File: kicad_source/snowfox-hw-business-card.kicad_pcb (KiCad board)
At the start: 2 copper layers, 85 x 54 mm, 114 parts, among them CN1 MEM2061-01-188-00-A, CN2 FSH-105-04-L-DH-SL, CN3 SFV24R-3STBE1HLF, CN4 10118192-0001LF, CN5 CONN_01X14, CN6 CONN_01X04, Q1 SI1308EDL, Q2 BC847, SW1 PTS 647 SK38 SMTR2 LFS, SW2 TAST_VER, SW3 PTS636 SL43 SMTR LFS, SW4 PTS 647 SK38 SMTR2 LFS, SW5 SWITCH_INV, U1 W25Q80D, U2 ATECC608A, U3 FE310-G002, U4 FT230XS, U5 TPS73633DBV, U6 TPS73618DBV, U7 M24LR, U8 BMA253, Y1 FA-238 16.0000MB-C3

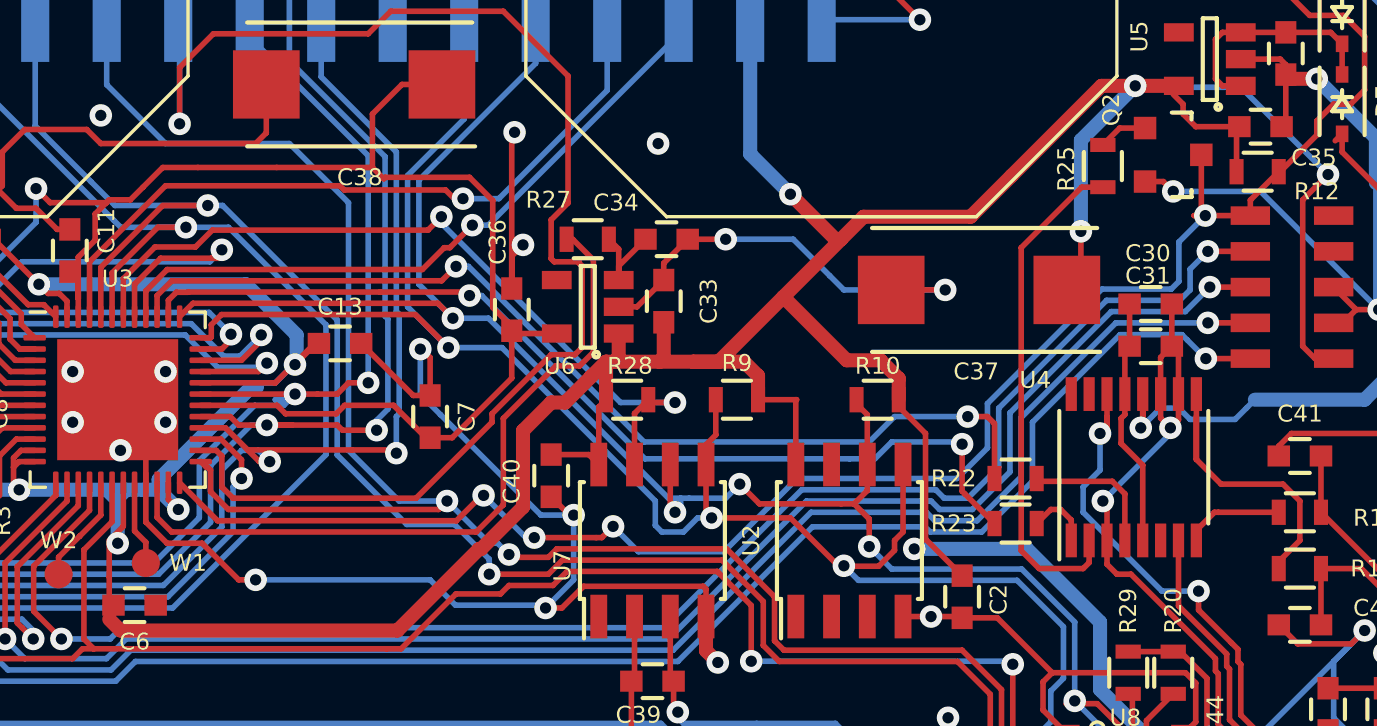
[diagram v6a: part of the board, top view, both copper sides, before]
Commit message: reworked reset circuit at usb serial
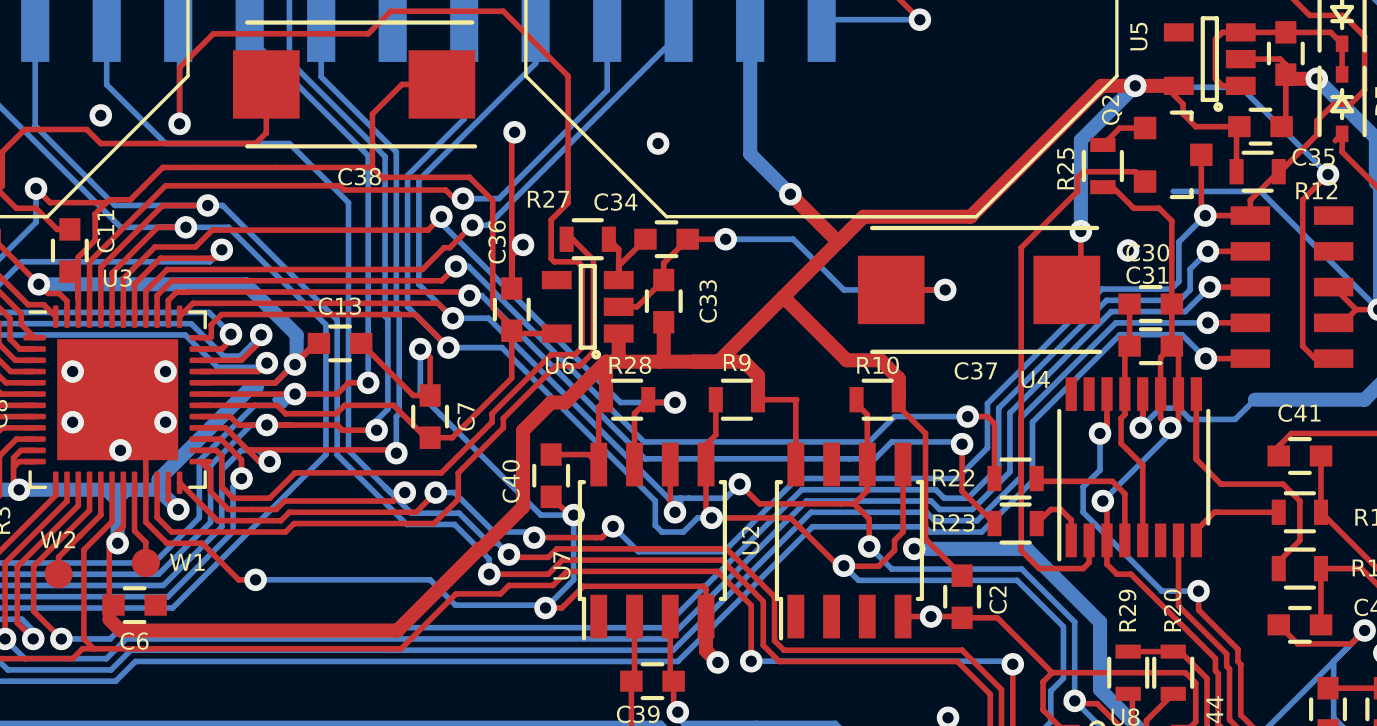
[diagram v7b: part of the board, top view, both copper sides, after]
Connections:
- Q2 pad 2: GND -> /USB/RTS
- R25 pad 1: /USB/RTS -> VIO
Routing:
- net VIO: track 48.9 -> 54.8 mm
- net /USB/RTS: track 18.1 -> 20.3 mm
- net GND: track 297.5 -> 296.4 mm
- net VDD_CORE_EN: track 25.9 -> 24.9 mm
- net /Microcontroller/LED: track 78.2 -> 77.6 mm
- net RESET: track 75.9 -> 75.4 mm

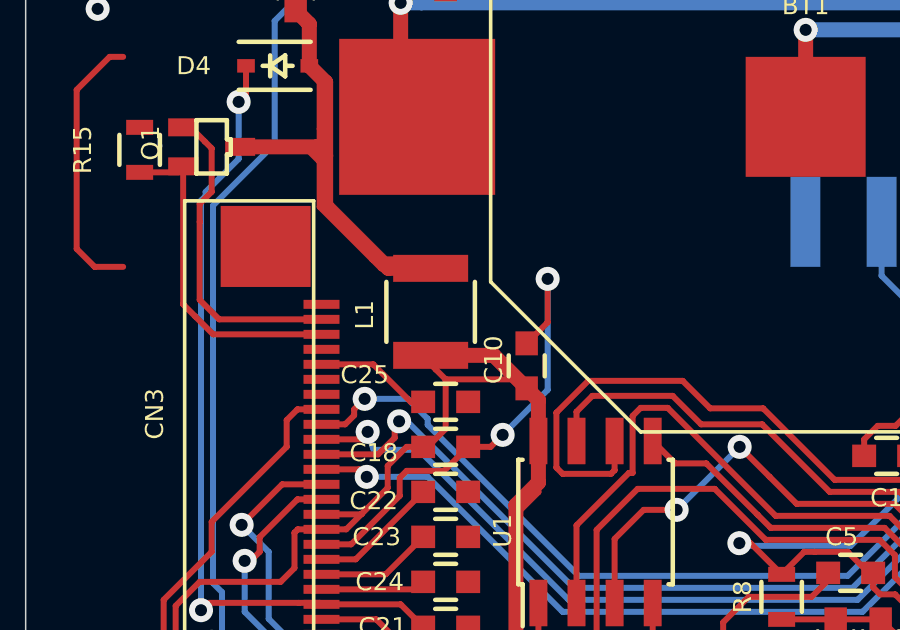
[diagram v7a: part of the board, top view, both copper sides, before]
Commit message: added C45 to pin4 of display
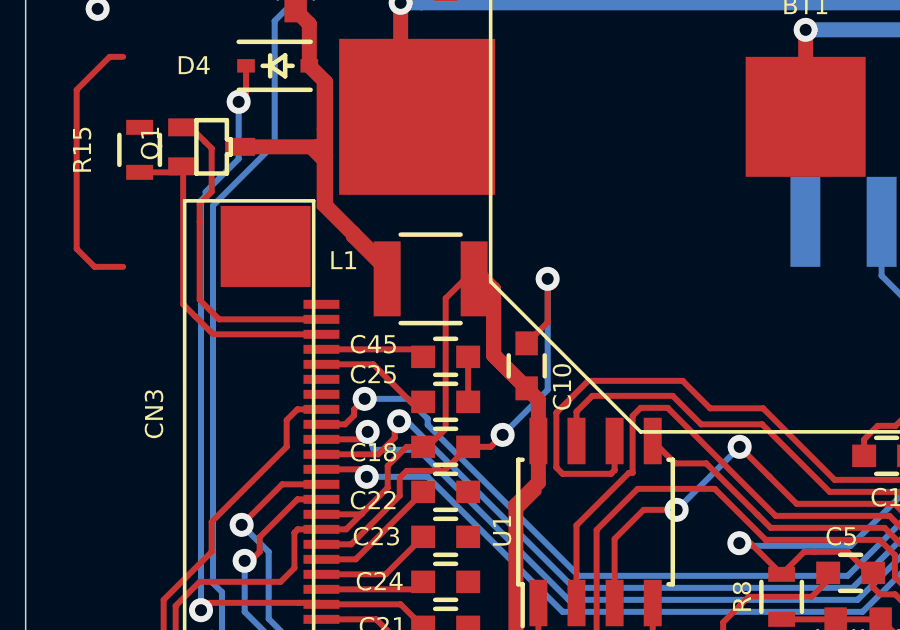
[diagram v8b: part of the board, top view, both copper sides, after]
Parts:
- added C45: 1uF 50V, capacitors:C_0603, F.Cu at (92.0, 101.0)
- moved L1 1.10 mm to (91.5, 98.4), turned to 180 degrees
- renumbered MECH3 to MECH2, MECH4 to MECH3, MECH5 to MECH4
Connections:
- net SPI_MISO renamed /Microcontroller/SPI_MISO
- CN3 pad 4: (no net) -> /Display/VGL2
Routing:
- net +3V3: track 346.3 -> 352.7 mm
- net /Display/VGL2: track 0.00 -> 3.49 mm
- net Net-(C20-Pad2): track 29.5 -> 26.1 mm
- net GND: track 296.4 -> 297.9 mm
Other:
- board text added: "find all information on this project at https://github.com/snowfox-project/snowfox-hw-business-card"
